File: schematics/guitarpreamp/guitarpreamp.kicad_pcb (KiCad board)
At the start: 2 copper layers, 90.8 x 58.4 mm, 61 parts, among them J1 10k Pot, J2 Conn_01x07_Female, J3 Phones, Line Out, Line In, Mi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, J4 Power Input, U1 9V Linear Regulator, U2 TL072, U3 5V Linear Regulator, U4 3.3V Digital, U5 3.3V Analog, U6 WM8731SEDS, Y1 12.288MHz

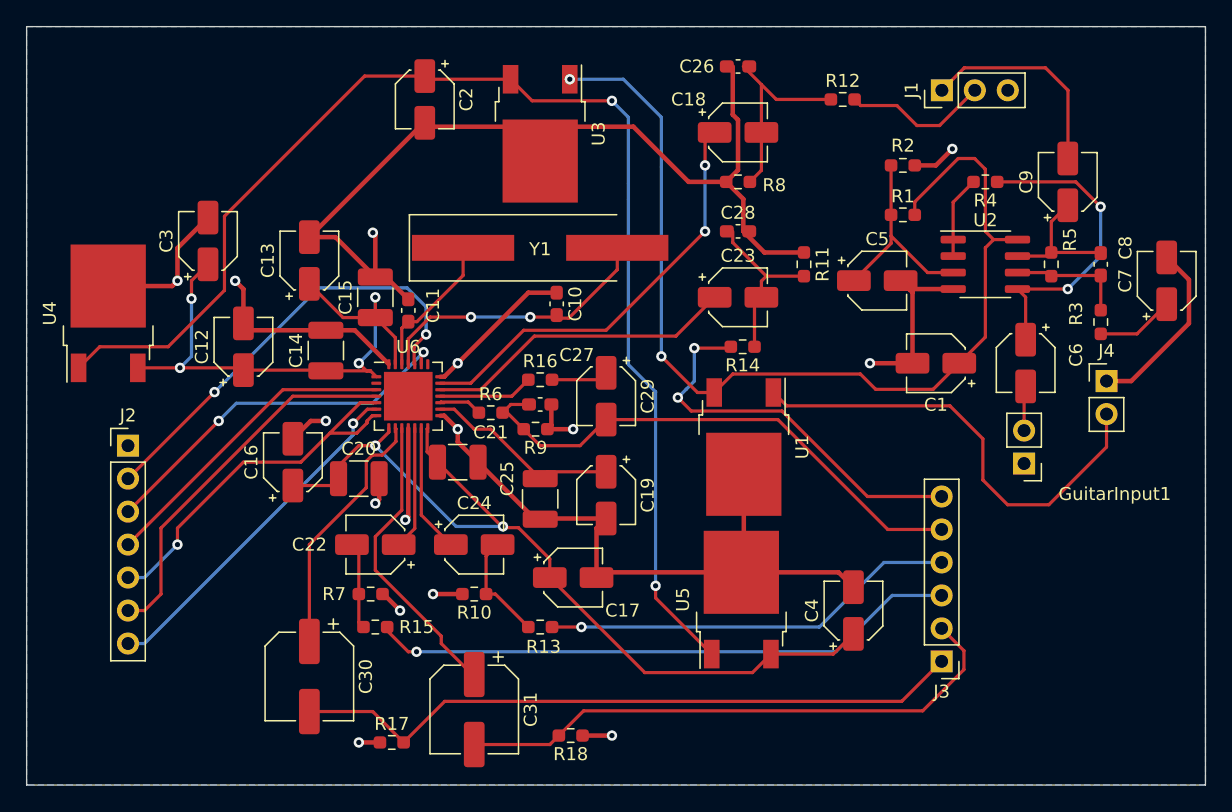
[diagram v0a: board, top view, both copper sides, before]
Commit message: schematics
* moved fritzing schematics to schematics folder
* updated pcb
* adapted gitignore
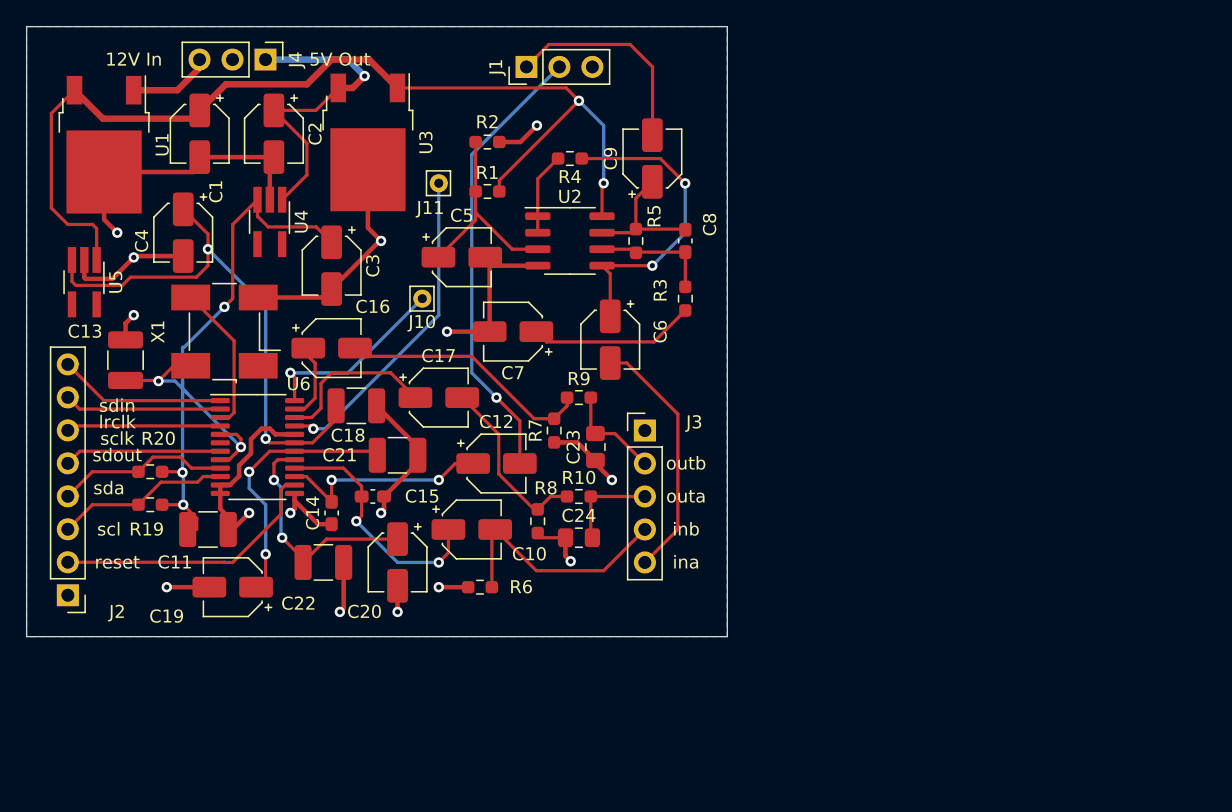
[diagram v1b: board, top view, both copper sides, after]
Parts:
- removed C25: 0.1uF, Capacitor_SMD:C_1210_3225Metric_Pad1.33x2.70mm_HandSolder
- removed C26, C27, C28: 220pF, Capacitor_SMD:C_0603_1608Metric_Pad1.08x0.95mm_HandSolder
- removed C29: 1uF, Capacitor_SMD:CP_Elec_4x4.5
- removed C30, C31: 220uF, Capacitor_SMD:CP_Elec_6.3x7.7
- removed GuitarInput1: Conn_01x02_Female, Connector_PinHeader_2.54mm:PinHeader_1x02_P2.54mm_Vertical
- removed R11, R12, R14: 5k6, Resistor_SMD:R_0603_1608Metric_Pad0.98x0.95mm_HandSolder
- removed R13, R15: 100, Resistor_SMD:R_0603_1608Metric_Pad0.98x0.95mm_HandSolder
- removed R16: 10k, Resistor_SMD:R_0603_1608Metric_Pad0.98x0.95mm_HandSolder
- removed R17, R18: 47k, Resistor_SMD:R_0603_1608Metric_Pad0.98x0.95mm_HandSolder
- removed Y1: 12.288MHz, Crystal:Crystal_SMD_HC49-SD_HandSoldering
- added J10: Conn_01x01_Female, Connector_Pin:Pin_D0.7mm_L6.5mm_W1.8mm_FlatFork, F.Cu at (59.7, 52.1)
- added J11: Conn_01x01_Female, Connector_Pin:Pin_D0.7mm_L6.5mm_W1.8mm_FlatFork, F.Cu at (61.0, 43.2)
- added R19: 2k2, Resistor_SMD:R_0603_1608Metric_Pad0.98x0.95mm_HandSolder, F.Cu at (38.7, 67.9)
- added R20: 2k2, Resistor_SMD:R_0603_1608Metric_Pad0.98x0.95mm_HandSolder, F.Cu at (38.7, 65.4)
- added X1: SG-5032CAN, Oscillator:Oscillator_SMD_SeikoEpson_SG8002CA-4Pin_7.0x5.0mm_HandSoldering, F.Cu at (44.5, 54.6)
- C10: value 22pF -> 10uF; footprint Capacitor_SMD:C_0603_1608Metric_Pad1.08x0.95mm_HandSolder -> Capacitor_SMD:CP_Elec_4x4.5
- C11: value 22pF -> 0.1uF; footprint Capacitor_SMD:C_0603_1608Metric_Pad1.08x0.95mm_HandSolder -> Capacitor_SMD:C_1210_3225Metric_Pad1.33x2.70mm_HandSolder
- C13, C18: value 10uF -> 0.1uF; footprint Capacitor_SMD:CP_Elec_4x4.5 -> Capacitor_SMD:C_1210_3225Metric_Pad1.33x2.70mm_HandSolder
- C14, C15: value 0.1uF -> 220pF; footprint Capacitor_SMD:C_1210_3225Metric_Pad1.33x2.70mm_HandSolder -> Capacitor_SMD:C_0603_1608Metric_Pad1.08x0.95mm_HandSolder
- C16, C17: value 10uF -> 3.3uF
- C19: value 10uF -> 47uF
- C20: value 0.1uF -> 10uF; footprint Capacitor_SMD:C_1210_3225Metric_Pad1.33x2.70mm_HandSolder -> Capacitor_SMD:CP_Elec_4x4.5
- C22: value 1uF -> 0.1uF; footprint Capacitor_SMD:CP_Elec_4x4.5 -> Capacitor_SMD:C_1210_3225Metric_Pad1.33x2.70mm_HandSolder
- C23: value 10uF -> 3.3nF; footprint Capacitor_SMD:CP_Elec_4x4.5 -> Capacitor_SMD:C_0805_2012Metric_Pad1.18x1.45mm_HandSolder
- C24: value 1uF -> 3.3nF; footprint Capacitor_SMD:CP_Elec_4x4.5 -> Capacitor_SMD:C_0805_2012Metric_Pad1.18x1.45mm_HandSolder
- C8: value 22pF -> 220pF
- J2: value Conn_01x07_Female -> Conn_01x08_Female; footprint Connector_PinHeader_2.54mm:PinHeader_1x07_P2.54mm_Vertical -> Connector_PinHeader_2.54mm:PinHeader_1x08_P2.54mm_Vertical
- J3: value Phones, Line Out, Line In, Mic In -> Conn_01x05_Female; footprint Connector_PinHeader_2.54mm:PinHeader_1x06_P2.54mm_Vertical -> Connector_PinHeader_2.54mm:PinHeader_1x05_P2.54mm_Vertical
- J4: value Power Input -> Conn_01x03_Female; footprint Connector_PinHeader_2.54mm:PinHeader_1x02_P2.54mm_Vertical -> Connector_PinHeader_2.54mm:PinHeader_1x03_P2.54mm_Vertical
- R10: value 47k -> 470
- R6: value 680 -> 47k
- R7: value 47k -> 10k
- R8: value 5k6 -> 10k
- R9: value 4k7 -> 470
- U4: footprint Package_TO_SOT_SMD:TO-252-2 -> Package_TO_SOT_SMD:TSOT-23-5_HandSoldering
- U5: value 3.3V Analog -> 5V Analog; footprint Package_TO_SOT_SMD:TO-252-2 -> Package_TO_SOT_SMD:TSOT-23-5_HandSoldering
- U6: value WM8731SEDS -> CS4270-CZZ; footprint Package_DFN_QFN:QFN-28-1EP_5x5mm_P0.5mm_EP3.75x3.75mm -> Package_SO:TSSOP-24_4.4x7.8mm_P0.65mm
- moved J4 69.4 mm to (47.6, 33.7), turned to -90 degrees
- moved C1 59.4 mm to (42.5, 39.4), turned to -90 degrees
- moved C4 59.3 mm to (41.3, 47.0), turned to -90 degrees
- moved U5 56.2 mm to (33.7, 50.8), turned to -90 degrees
- moved U1 54.5 mm to (35.2, 40.2)
- moved C7 50.5 mm to (66.7, 54.6), turned to 180 degrees
- moved C18 36.2 mm to (54.6, 60.3), turned to 180 degrees
- moved C5 32.1 mm to (62.7, 48.9)
- moved C6 32.1 mm to (74.2, 55.2)
- moved C8 32.1 mm to (80.0, 47.6)
- moved C9 32.1 mm to (77.4, 41.3)
- moved J1 32.1 mm to (67.7, 34.2)
- moved R1 32.1 mm to (64.7, 43.8)
- moved R2 32.1 mm to (64.7, 40.0)
- moved R3 32.1 mm to (80.0, 52.1)
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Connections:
- C10 pad 1: GND -> Net-(C10-Pad1)
- C12 pad 2: GND -> Net-(C12-Pad2)
- C13 pad 1: Net-(C12-Pad1) -> Net-(C11-Pad1)
- C14 pad 1: Net-(C12-Pad1) -> GND
- C14 pad 2: GND -> Net-(C12-Pad1)
- C15 pad 1: Net-(C12-Pad1) -> GND
- C15 pad 2: GND -> Net-(C10-Pad1)
- C16 pad 2: GND -> Net-(C16-Pad2)
- C17 pad 1: Net-(C16-Pad1) -> Net-(C17-Pad1)
- C17 pad 2: GND -> Net-(C17-Pad2)
- C18 pad 1: Net-(C18-Pad1) -> GND
- C2 pad 1: +5V -> Net-(C2-Pad1)
- C20 pad 1: Net-(C16-Pad1) -> Net-(C20-Pad1)
- C21 pad 1: Net-(C16-Pad1) -> GND
- C21 pad 2: GND -> Net-(C19-Pad1)
- C22 pad 1: Net-(C22-Pad1) -> Net-(C20-Pad1)
- C22 pad 2: Net-(C22-Pad2) -> GND
- C23 pad 1: Net-(C23-Pad1) -> GND
- C24 pad 1: Net-(C24-Pad1) -> GND
- C3 pad 1: Net-(C12-Pad1) -> Net-(C11-Pad1)
- C4 pad 1: Net-(C16-Pad1) -> Net-(C18-Pad2)
- J1 pad 2: Net-(J1-Pad2) -> Net-(C12-Pad2)
- J3 pad 1: Net-(C30-Pad2) -> GND
- J3 pad 2: Net-(C31-Pad2) -> Net-(C23-Pad2)
- J3 pad 3: Net-(J3-Pad3) -> Net-(C24-Pad2)
- J3 pad 4: Net-(J3-Pad4) -> Net-(C10-Pad2)
- J3 pad 5: Net-(C27-Pad1) -> Net-(C6-Pad2)
- J4 pad 1: GND -> Net-(C2-Pad1)
- J4 pad 2: +12V -> GND
- R10 pad 1: Net-(C24-Pad2) -> Net-(C17-Pad2)
- R10 pad 2: GND -> Net-(C24-Pad2)
- R6 pad 1: Net-(R6-Pad1) -> GND
- R6 pad 2: Net-(C27-Pad1) -> Net-(C10-Pad2)
- R7 pad 1: Net-(C22-Pad2) -> GND
- R7 pad 2: GND -> Net-(C16-Pad2)
- R8 pad 2: Net-(C18-Pad2) -> Net-(C17-Pad2)
- R9 pad 1: GND -> Net-(C16-Pad2)
- R9 pad 2: Net-(C27-Pad1) -> Net-(C23-Pad2)
- U3 pad 3: +5V -> Net-(C2-Pad1)
- U4 pad 1: +5V -> Net-(C2-Pad1)
- U4 pad 3: Net-(C12-Pad1) -> Net-(C11-Pad1)
- U5 pad 1: +5V -> +9V
- U5 pad 3: Net-(C16-Pad1) -> Net-(C18-Pad2)
- U6 pad 1: Net-(C12-Pad1) -> Net-(J2-Pad8)
- U6 pad 10: Net-(C31-Pad1) -> Net-(J2-Pad3)
- U6 pad 12: Net-(C22-Pad1) -> GND
- U6 pad 13: Net-(C24-Pad1) -> GND
- U6 pad 14: Net-(C16-Pad1) -> Net-(J2-Pad2)
- U6 pad 15: GND -> Net-(C12-Pad1)
- U6 pad 16: Net-(C19-Pad1) -> Net-(C10-Pad1)
- U6 pad 17: Net-(R6-Pad1) -> Net-(C20-Pad1)
- U6 pad 18: Net-(R16-Pad1) -> Net-(C19-Pad1)
- U6 pad 19: Net-(C23-Pad1) -> Net-(C18-Pad2)
- U6 pad 2: unconnected-(U6-Pad2) -> Net-(J2-Pad7)
- U6 pad 20: Net-(C18-Pad1) -> GND
- U6 pad 21: GND -> Net-(U6-Pad21)
- U6 pad 22: unconnected-(U6-Pad22) -> Net-(C17-Pad1)
- U6 pad 23: Net-(J2-Pad3) -> Net-(C16-Pad1)
- U6 pad 24: Net-(J2-Pad2) -> Net-(U6-Pad24)
- U6 pad 3: Net-(J2-Pad4) -> Net-(U6-Pad3)
- U6 pad 5: Net-(J2-Pad5) -> Net-(C11-Pad1)
- U6 pad 6: Net-(J2-Pad7) -> unconnected-(U6-Pad6)
- U6 pad 8: Net-(C16-Pad1) -> Net-(C11-Pad1)
- U6 pad 9: Net-(C30-Pad1) -> Net-(J2-Pad4)
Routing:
- net +5V: track 100.3 -> 0.00 mm, vias 2 -> 0
- net GND: track 215.6 -> 118.1 mm
- net Net-(C16-Pad1): track 66.2 -> 5.37 mm, vias 2 -> 0
- net Net-(C30-Pad2): track 52.3 -> 0.00 mm
- net Net-(C11-Pad1): track 11.3 -> 59.3 mm, vias 0 -> 5
- net Net-(J3-Pad3): track 45.5 -> 0.00 mm, vias 1 -> 0
- net Net-(C31-Pad2): track 44.0 -> 0.00 mm
- net Net-(C27-Pad1): track 41.5 -> 0.00 mm
- net Net-(C12-Pad2): track 0.00 -> 34.9 mm, vias 0 -> 1
- net Net-(C18-Pad1): track 33.2 -> 0.00 mm, vias 2 -> 0
- net Net-(J3-Pad4): track 32.1 -> 0.00 mm, vias 1 -> 0
- net Net-(J3-Pad6): track 30.7 -> 0.00 mm, vias 2 -> 0
- net +12V: track 35.5 -> 5.80 mm
- net Net-(C12-Pad1): track 46.2 -> 16.8 mm, vias 4 -> 2
- net Net-(C18-Pad2): track 15.7 -> 41.2 mm, vias 0 -> 2
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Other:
- board size 90.8 x 58.4 mm -> 54 x 47 mm
- board text added: "12V In"
- board text added: "5V Out"
- board text added: "ina"
- board text added: "inb"
- board text added: "lrclk"
- board text added: "outa"
- board text added: "outb"
- board text added: "reset"
- board text added: "scl"
- board text added: "sclk"
- board text added: "sda"
- board text added: "sdin"
- board text added: "sdout"

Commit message: corrected some design mistakes
* connected oscillator enable to reset
* attached DGND
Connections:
- J2 pad 2: Net-(J2-Pad2) -> Net-(X1-Pad1)
- U6 pad 14: Net-(J2-Pad2) -> Net-(X1-Pad1)
- U6 pad 6: unconnected-(U6-Pad6) -> GND
- X1 pad 1: unconnected-(X1-Pad1) -> Net-(X1-Pad1)
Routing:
- net Net-(X1-Pad1): track 0.00 -> 52.0 mm, vias 0 -> 3
- net Net-(J2-Pad2): track 21.2 -> 0.00 mm
- net GND: track 118.1 -> 119.8 mm, vias 15 -> 16

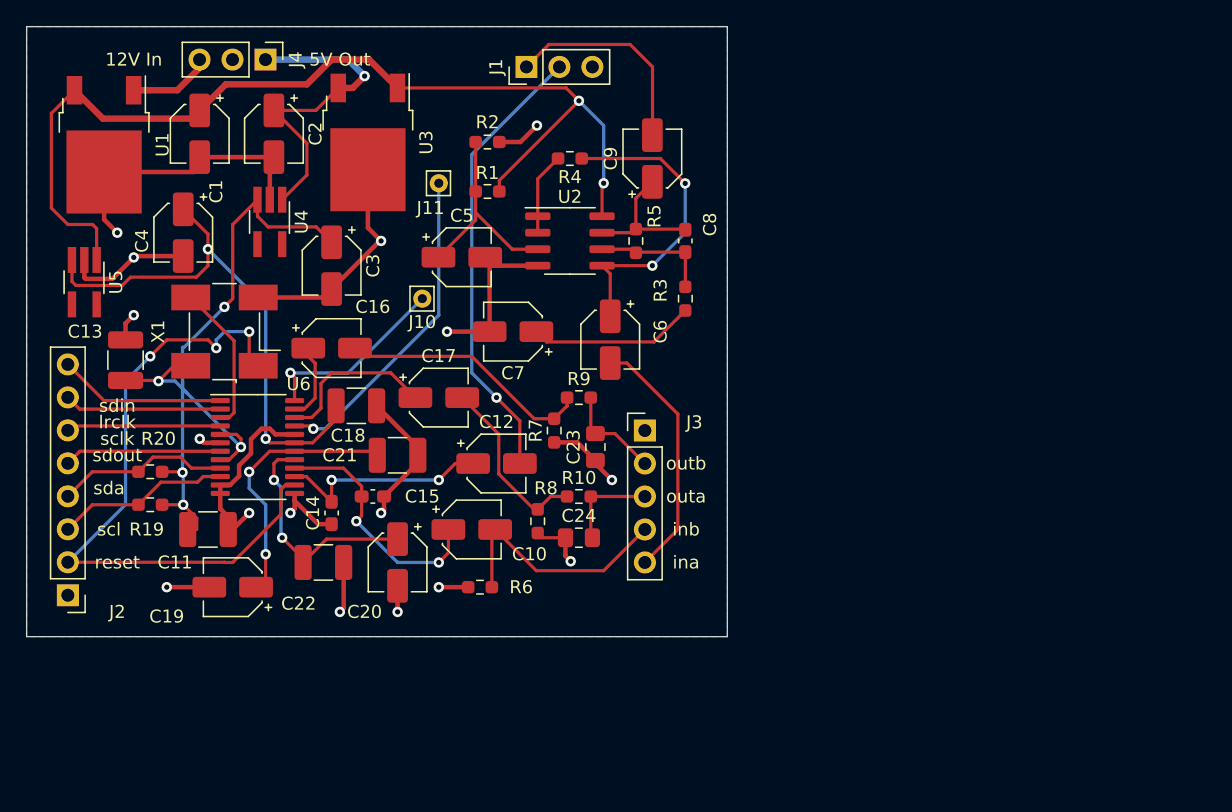
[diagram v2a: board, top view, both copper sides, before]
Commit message: changed regulators, added design fixes
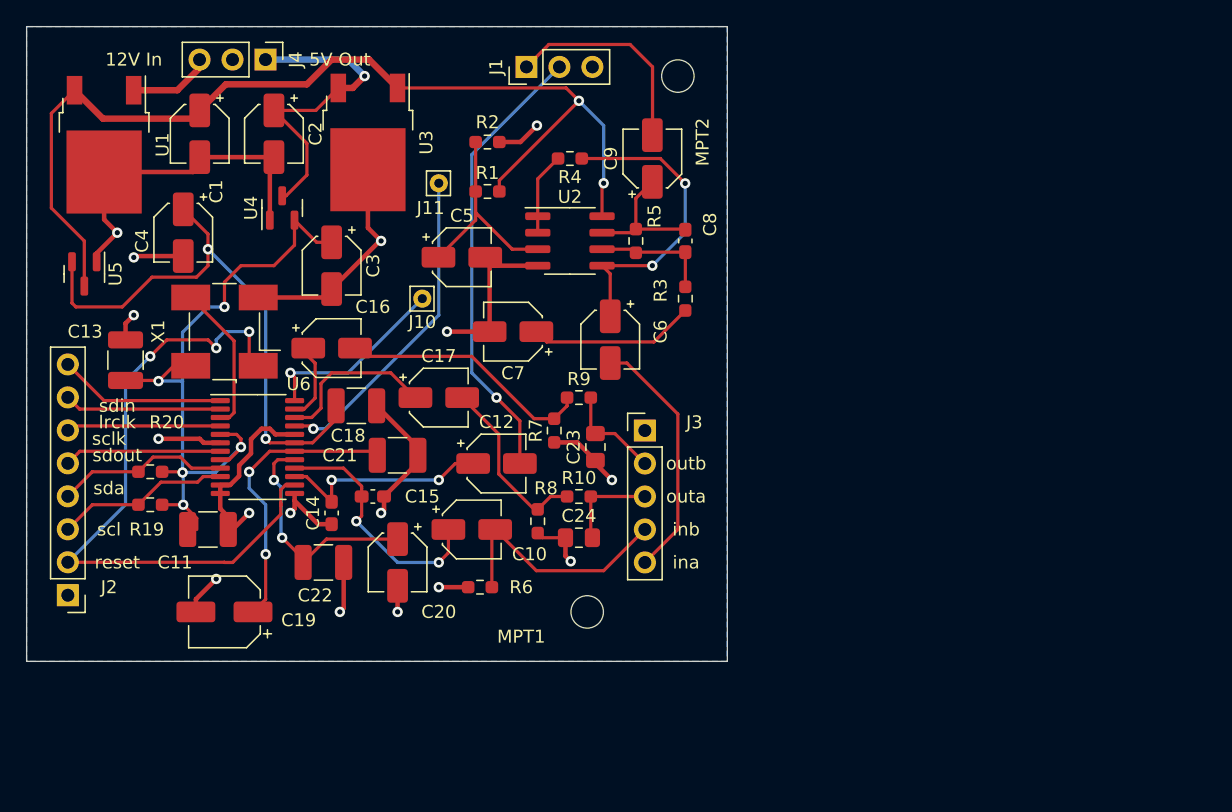
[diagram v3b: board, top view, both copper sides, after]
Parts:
- added MPT1: MountingHole_2.5mm, MountingHole:MountingHole_2.5mm, F.Cu at (72.4, 76.2)
- added MPT2: MountingHole_2.5mm, MountingHole:MountingHole_2.5mm, F.Cu at (79.4, 34.9)
- C19: footprint Capacitor_SMD:CP_Elec_4x4.5 -> Capacitor_SMD:CP_Elec_5x5.4
- U4: value 3.3V Digital -> 3.3v Digital; footprint Package_TO_SOT_SMD:TSOT-23-5_HandSoldering -> Package_TO_SOT_SMD:SOT-23
- U5: value 5V Analog -> 5v Analog; footprint Package_TO_SOT_SMD:TSOT-23-5_HandSoldering -> Package_TO_SOT_SMD:SOT-23
- moved C19 2.01 mm to (44.5, 76.2)
- moved U4 1.43 mm to (48.9, 45.1), turned to 90 degrees
- moved U5 0.63 mm to (33.7, 50.2)
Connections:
- U4 pad 1: Net-(C2-Pad1) -> GND
- U4 pad 2: GND -> Net-(C11-Pad1)
- U4 pad 3: Net-(C11-Pad1) -> Net-(C2-Pad1)
- U5 pad 1: +9V -> GND
- U5 pad 2: GND -> Net-(C18-Pad2)
- U5 pad 3: Net-(C18-Pad2) -> +9V
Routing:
- net Net-(C11-Pad1): track 59.3 -> 54.5 mm
- net Net-(C18-Pad2): track 41.2 -> 43.5 mm
- net Net-(C19-Pad1): track 21.1 -> 23.1 mm
- net GND: track 119.8 -> 121.5 mm
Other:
- board size 54 x 47 mm -> 54 x 48.9 mm

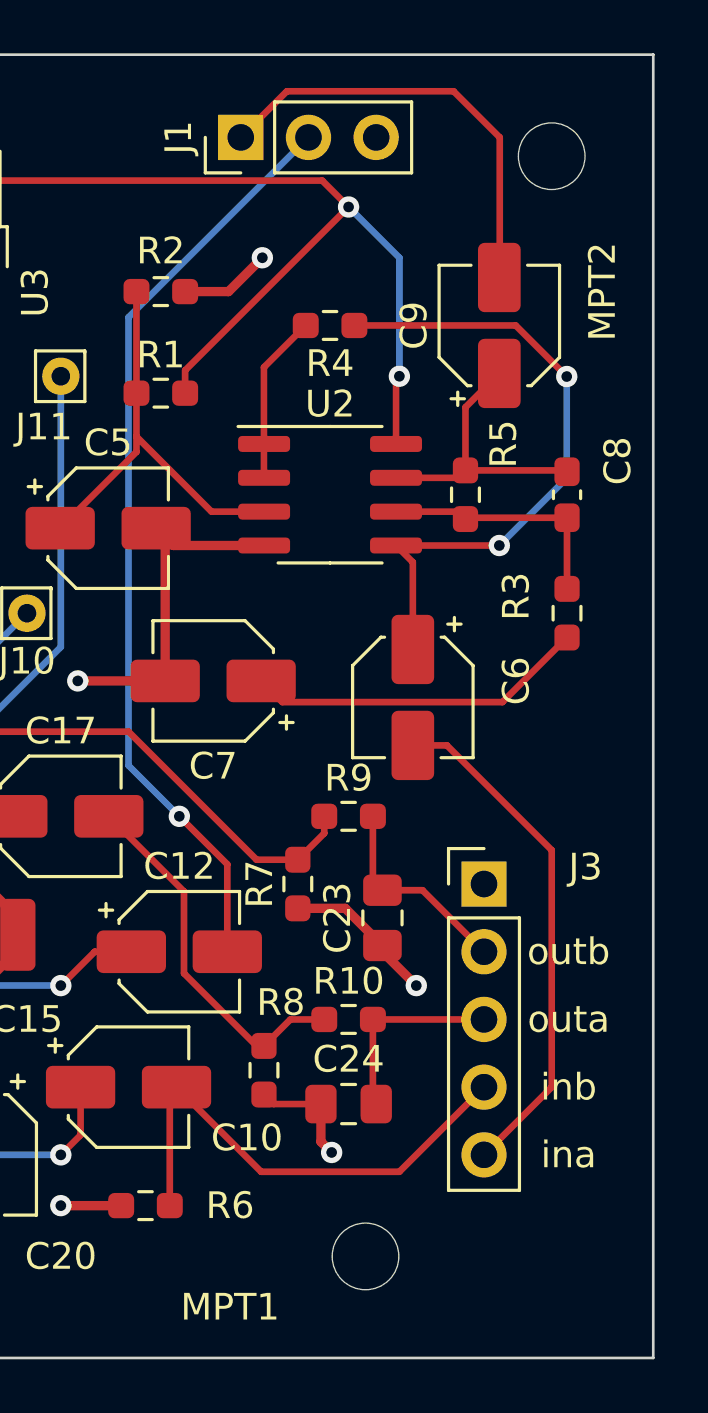
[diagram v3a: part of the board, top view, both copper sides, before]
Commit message: changed cab values
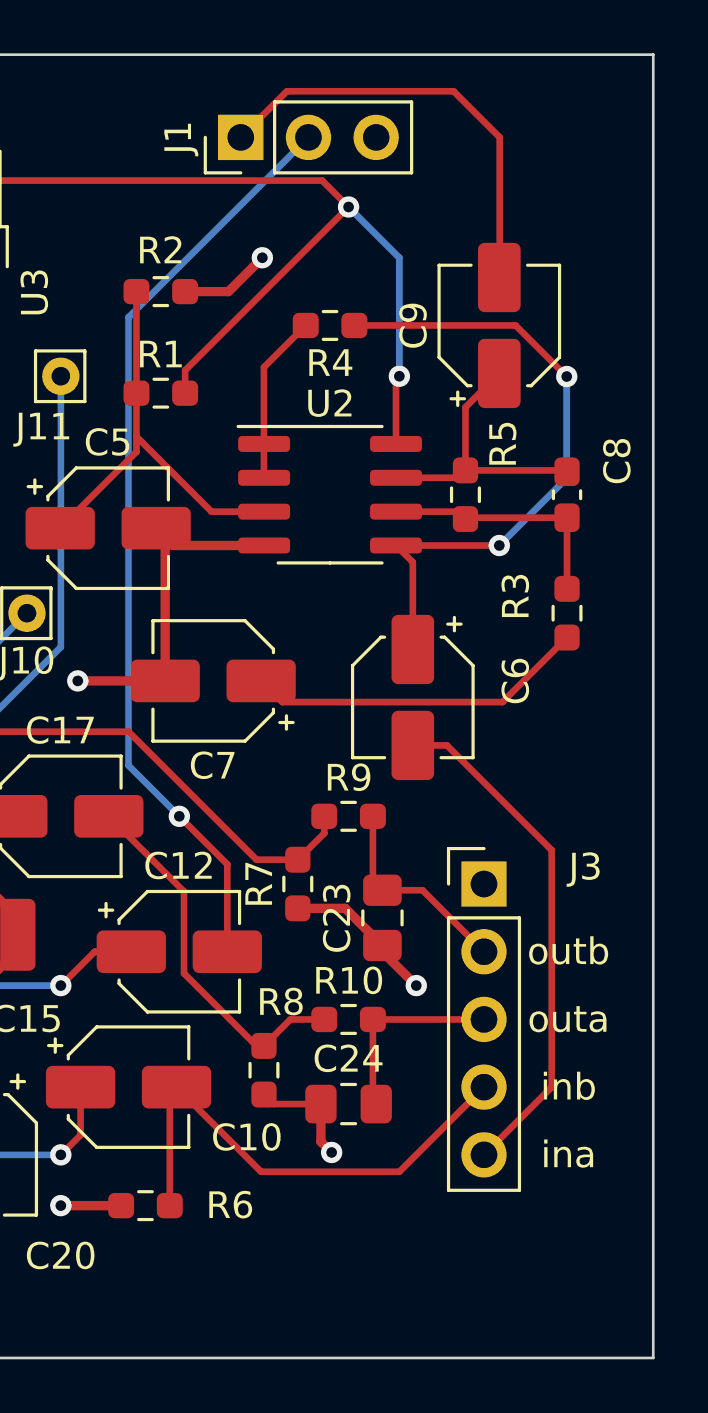
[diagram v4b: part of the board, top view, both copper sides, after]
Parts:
- removed MPT1, MPT2: MountingHole_2.5mm, MountingHole:MountingHole_2.5mm
- C7: value 1uF -> 4.7uF
